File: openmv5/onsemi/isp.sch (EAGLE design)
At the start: 58 parts, among them IC1 AP0202AT2L00XPGA0, IC2 MIC5365-2.8YC5-TR, IC3 TLV62568PDDCR, J1 DF12-36-DS, J2 DF12-36-DP, M1 9774030151R, M2 9774030151R, Q1 PMXB120EPEZ

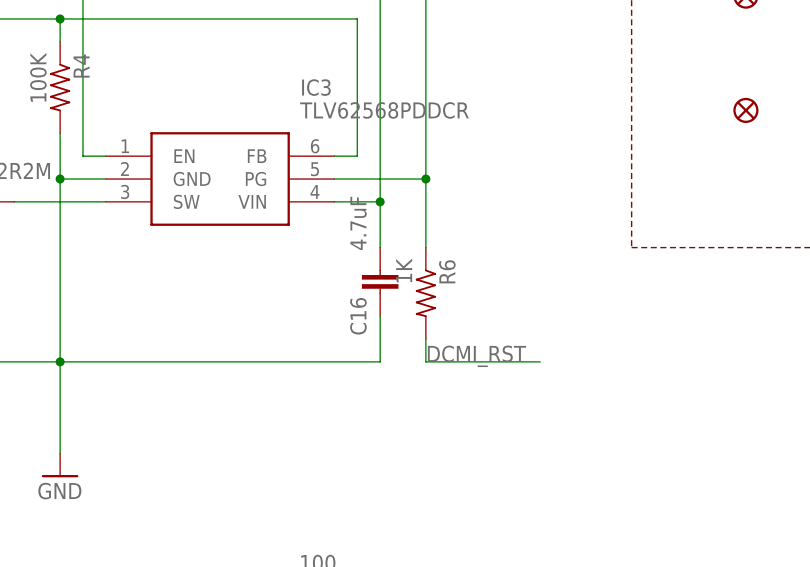
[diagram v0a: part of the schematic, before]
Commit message: Update resistor value
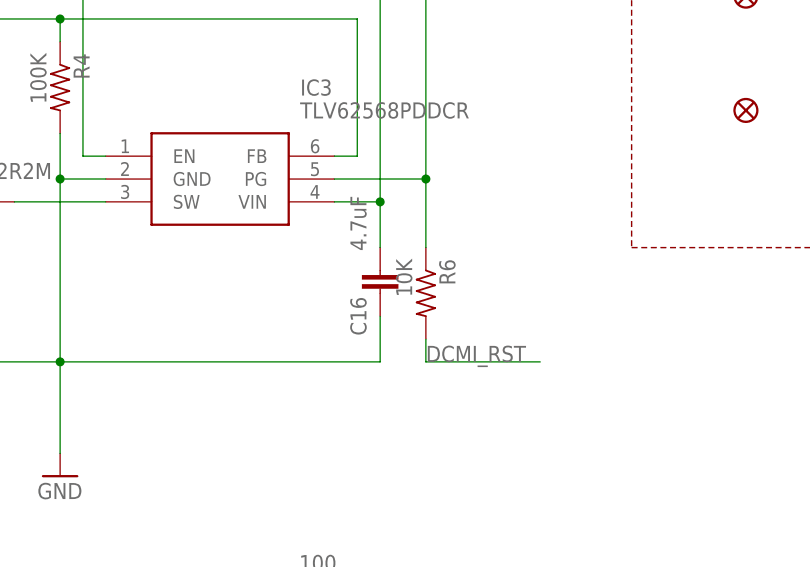
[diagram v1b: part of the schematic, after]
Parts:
- R6: value 1K -> 10K; MPN CRCW04021K00FKEDC -> AC0402FR-1310KL
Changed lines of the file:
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@@
 <attribute name="MPN" value="MFBM1V1005-101-R"/>
 </part>
-<part name="R6" library="rcl" library_urn="urn:adsk.eagle:library:334" deviceset="R-US_" device="R0402" package3d_urn="urn:adsk.eagle:package:23547/3" value="1K">
+<part name="R6" library="rcl" library_urn="urn:adsk.eagle:library:334" deviceset="R-US_" device="R0402" package3d_urn="urn:adsk.eagle:package:23547/3" value="10K">
 <spice>
 <pinmapping spiceprefix="R">
@@
 </pinmapping>
 </spice>
-<attribute name="MPN" value="CRCW04021K00FKEDC"/>
+<attribute name="MPN" value="AC0402FR-1310KL"/>
 </part>
 </parts>
